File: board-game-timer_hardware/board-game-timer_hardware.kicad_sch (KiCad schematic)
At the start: 29 parts, among them J1 Conn_01x05_Pin, J2 Conn_01x04_Pin, J3 Conn_01x04_Pin, J4 Conn_01x02_Pin, J5 USB_B_Micro, SW1 SW_B0, SW2 SW_RST, U1 AMS1117-3.3, U2 STM32F030F4Px, Y1 16MHz

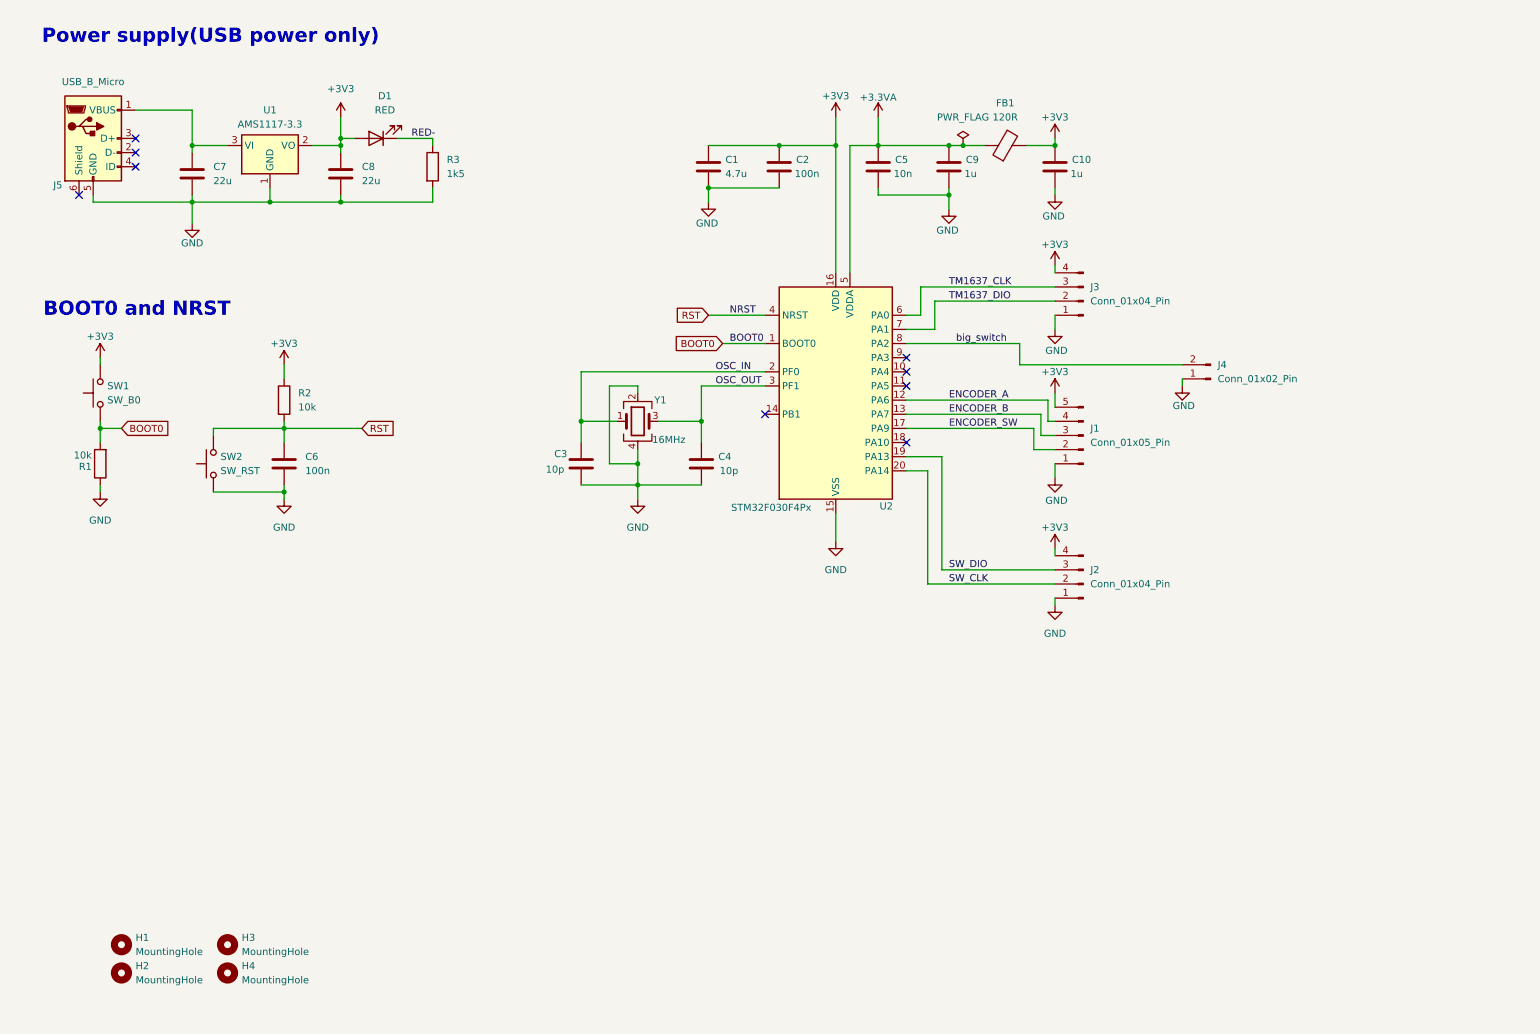
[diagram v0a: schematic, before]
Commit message: V1.1 work in progress
- Added symbols for display and ic, rewired everything for one pcb
- Added programmer header 2x10 for easier access
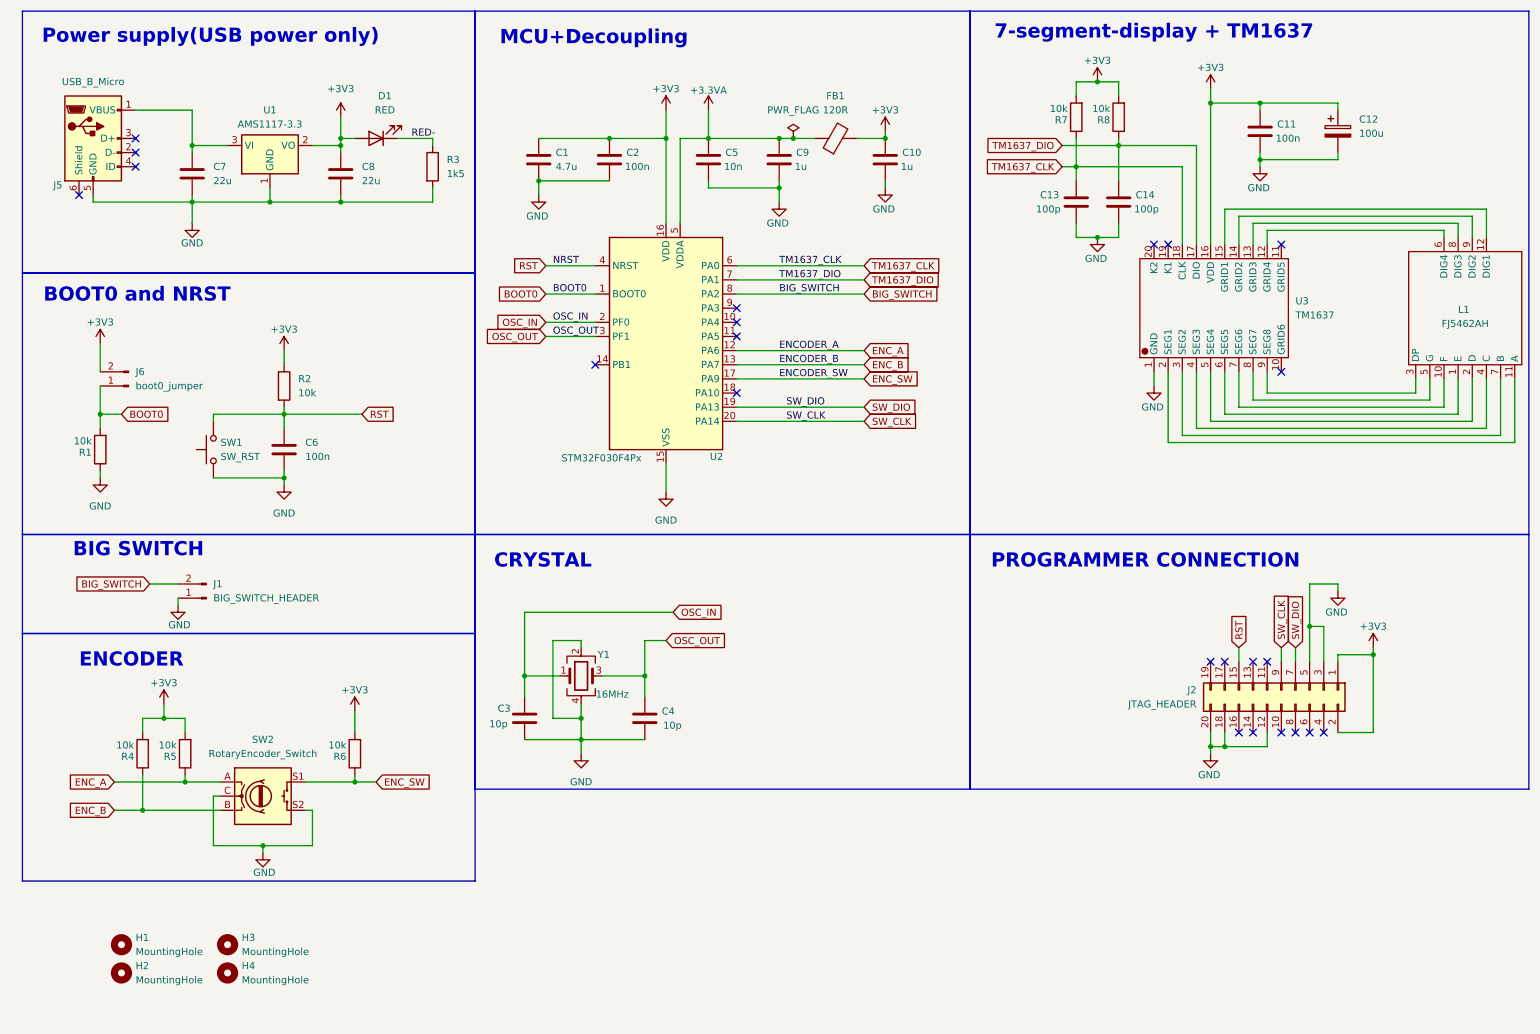
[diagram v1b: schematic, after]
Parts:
- removed J1: Conn_01x05_Pin, Connector_PinHeader_2.54mm:PinHeader_1x05_P2.54mm_Vertical, symbol Connector:Conn_01x05_Pin
- removed J2, J3: Conn_01x04_Pin, Connector_PinHeader_2.54mm:PinHeader_1x04_P2.54mm_Vertical, symbol Connector:Conn_01x04_Pin
- removed SW1: SW_B0, Button_Switch_THT:SW_PUSH_6mm, symbol Switch:SW_Push
- added C11: 100n, Capacitor_SMD:C_0402_1005Metric, symbol Device:C
- added C12: 100u, symbol Device:C_Polarized
- added C13, C14: 100p, Capacitor_SMD:C_0402_1005Metric, symbol Device:C
- added J2: JTAG_HEADER, symbol Connector_Generic:Conn_02x10_Odd_Even
- added J6: boot0_jumper, Connector_PinHeader_2.54mm:PinHeader_1x02_P2.54mm_Vertical, symbol Connector:Conn_01x02_Pin
- added L1: FJ5462AH, symbol My_own_components:ZHIHAO_FJ5462AH
- added R4, R5, R6, R7, R8: 10k, Resistor_SMD:R_0402_1005Metric, symbol Device:R
- added SW2: RotaryEncoder_Switch, symbol Device:RotaryEncoder_Switch
- added U3: TM1637, symbol My_own_components:TM1637
- J1: renamed from J4; value Conn_01x02_Pin -> BIG_SWITCH_HEADER
- renumbered SW2 to SW1
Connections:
- net +3V3: now also C11.1, C12.1, J2.1 (Pin_1), J2.2 (Pin_2), J6.2 (Pin_2), R4.2, R5.2, R6.2, R7.2, R8.2, U3.16 (VDD)
- net BOOT0: now also J6.1 (Pin_1)
- net GND: now also C11.2, C12.2, C13.2, C14.2, J2.12 (Pin_12), J2.18 (Pin_18), J2.20 (Pin_20), J2.3 (Pin_3), J2.5 (Pin_5), SW2.C, SW2.S2, U3.1 (GND)
- net RST: now also J2.15 (Pin_15)
- net SW_CLK: now also J2.9 (Pin_9)
- net SW_DIO: now also J2.7 (Pin_7)
- net TM1637_CLK: now also C13.1, R7.1, U3.18 (CLK)
- net TM1637_DIO: now also C14.1, R8.1, U3.17 (DIO)
- net ENCODER_A renamed ENC_A
- net ENC_A: now also R5.1, SW2.A
- net ENCODER_B renamed ENC_B
- net ENC_B: now also R4.1, SW2.B
- net ENCODER_SW renamed ENC_SW
- net ENC_SW: now also R6.1, SW2.S1
- net big_switch renamed BIG_SWITCH
- new net: L1.1 (E), U3.6 (SEG5)
- new net: L1.10 (F), U3.7 (SEG6)
- new net: L1.11 (A), U3.2 (SEG1)
- new net: L1.12 (DIG1), U3.15 (GRID1)
- new net: L1.2 (D), U3.5 (SEG4)
- new net: L1.3 (DP), U3.9 (SEG8)
- new net: L1.4 (C), U3.4 (SEG3)
- new net: L1.5 (G), U3.8 (SEG7)
- new net: L1.6 (DIG4), U3.12 (GRID4)
- new net: L1.7 (B), U3.3 (SEG2)
- new net: L1.8 (DIG3), U3.13 (GRID3)
- new net: L1.9 (DIG2), U3.14 (GRID2)
- no-connect marks 9 -> 23
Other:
- note added: "7-segment-display + TM1637"
- note added: "BIG SWITCH"
- note added: "CRYSTAL"
- note added: "ENCODER"
- note added: "MCU+Decoupling"
- note added: "PROGRAMMER CONNECTION"
- moved on the sheet: C1, C10, C2, C3, C4, C5, C6, C9, FB1, J1, R1, R2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

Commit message: PCB v1.1
- Moved encoder, screen on the pcb
- Added buzzer
- Changed layer stackup to SIG/GND/PWR/SIG
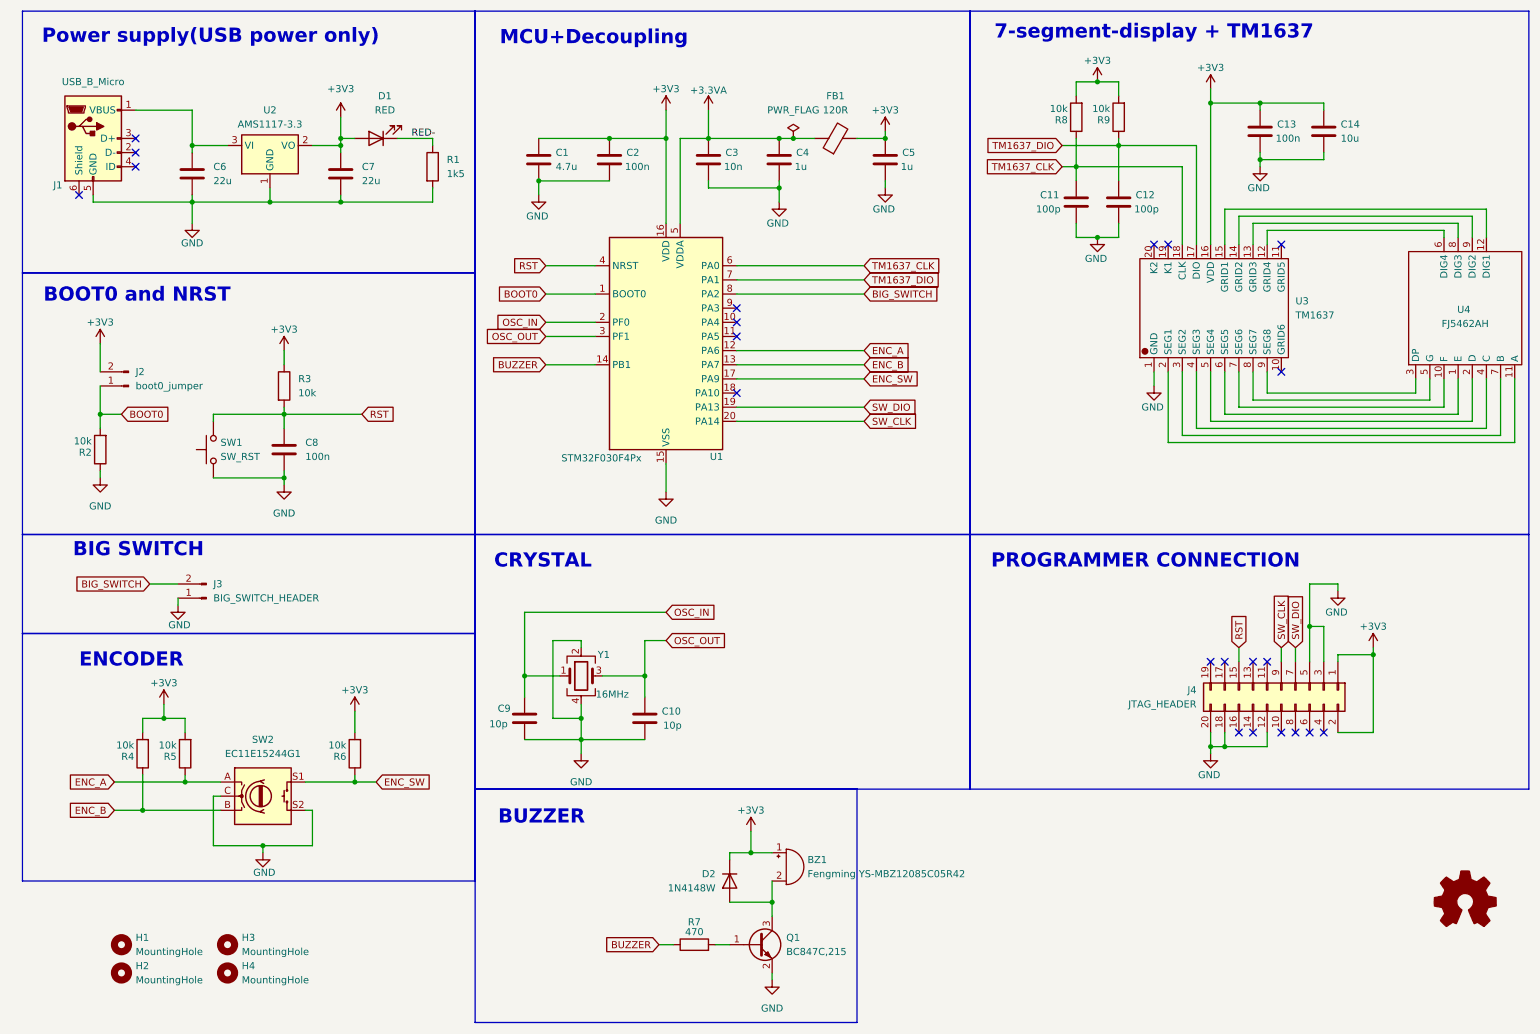
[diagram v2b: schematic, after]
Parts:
- removed C12: 100u, symbol Device:C_Polarized
- added BZ1: Fengming YS-MBZ12085C05R42, Buzzer_Beeper:Buzzer_12x9.5RM7.6, symbol Device:Buzzer
- added C14: 10u, Capacitor_SMD:C_0805_2012Metric, symbol Device:C
- added D2: 1N4148W, Diode_SMD:D_SOD-123, symbol Diode:1N4148W
- added Q1: BC847C,215, Package_TO_SOT_SMD:SOT-23-3, symbol Transistor_BJT:Q_NPN_BEC
- added R7: 470, Resistor_SMD:R_0402_1005Metric, symbol Device:R
- J4: renamed from J2; footprint (none) -> Connector_PinHeader_2.54mm:PinHeader_2x10_P2.54mm_Vertical
- SW2: value RotaryEncoder_Switch -> EC11E15244G1; footprint (none) -> Rotary_Encoder:RotaryEncoder_Alps_EC11E-Switch_Vertical_H20mm
- U3: footprint (none) -> My_own_components:TM1637
- U4: renamed from L1; footprint (none) -> My_own_components:ZHIHAO FJ5462AH
- renumbered C4 to C10, C13 to C11, C14 to C12, C11 to C13, C5 to C3, C9 to C4, C10 to C5, C7 to C6, C8 to C7, C6 to C8, C3 to C9, J5 to J1, J6 to J2, J1 to J3, R3 to R1, R1 to R2, R2 to R3, R7 to R8, R8 to R9, U2 to U1, U1 to U2
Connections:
- net +3V3: now also BZ1.1 (+), C14.1, D2.1 (K)
- net GND: now also C14.2, Q1.2 (E)
- net BUZZER: now reaches U1.14 (PB1)
- net BUZZER: now also R7.1
- new net: BZ1.2 (-), D2.2 (A), Q1.3 (C)
- new net: Q1.1 (B), R7.2
- no-connect marks 23 -> 22
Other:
- note added: "BUZZER"
